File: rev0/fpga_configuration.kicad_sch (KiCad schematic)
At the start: 40 parts, among them IC1 ECP5-BGA256, J10 TC_SWD, J5 Conn_FPGA_JTAG_10, J6 Conn_ARM_JTAG_SWD_10, U6 ATSAMD11D14A-MUT, U7 W25Q32JVSS

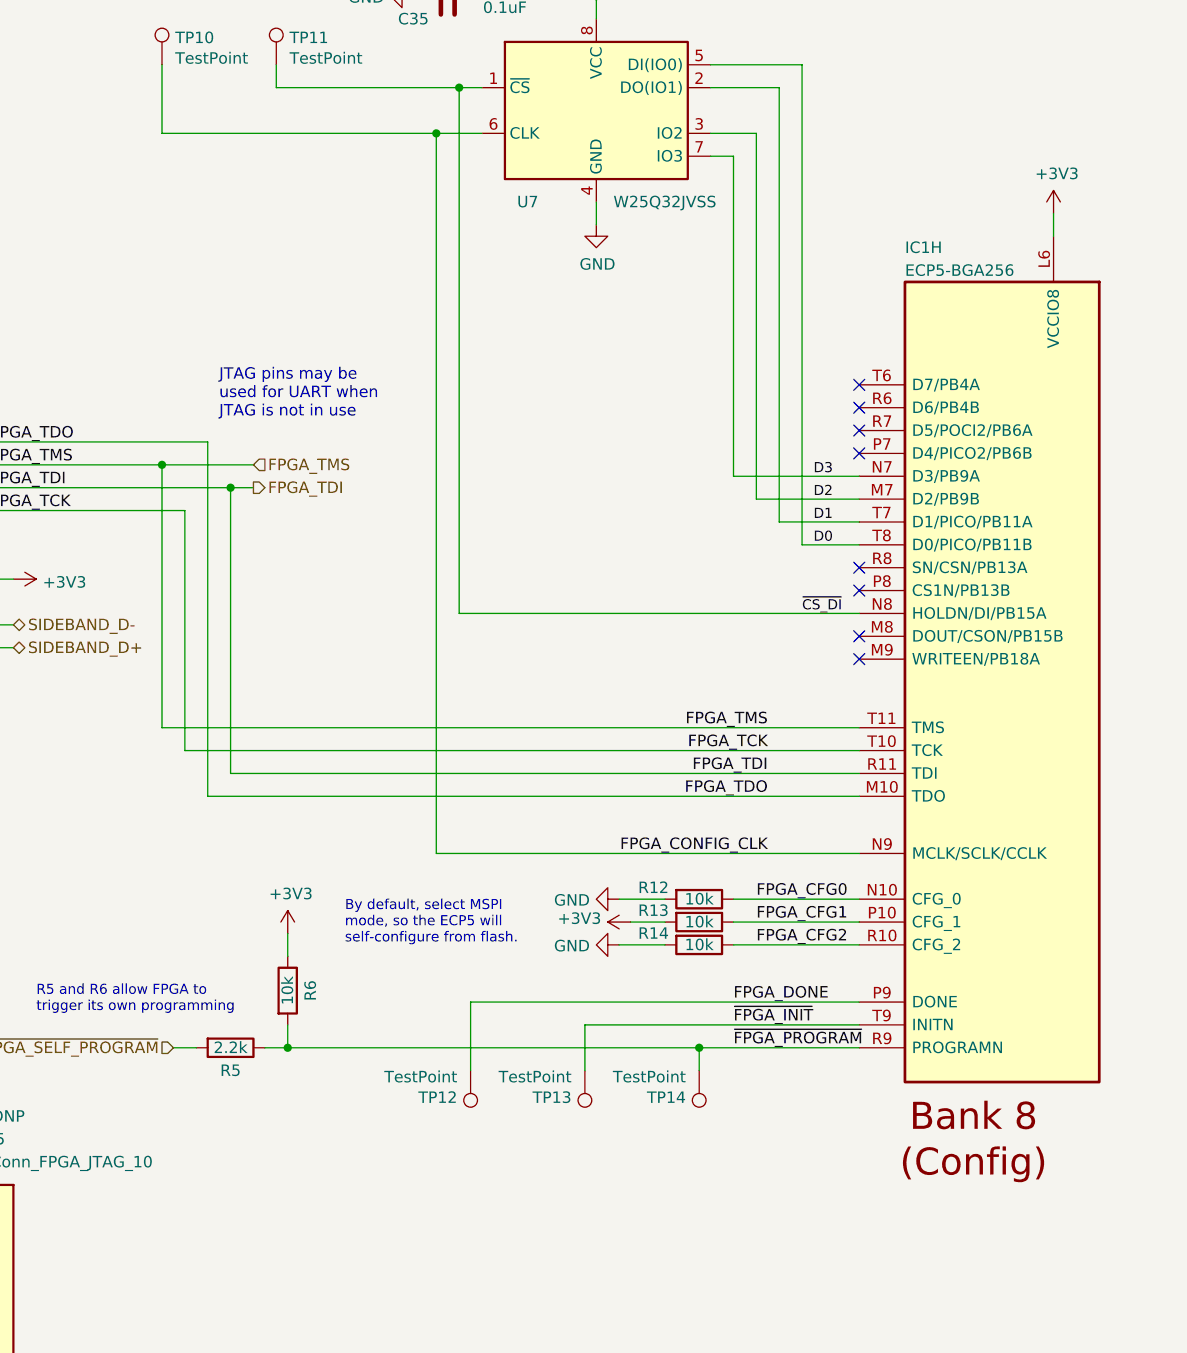
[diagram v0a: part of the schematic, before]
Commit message: hardware: add button BTN to FPGA
intended for SoC reset or alternative FPGA use
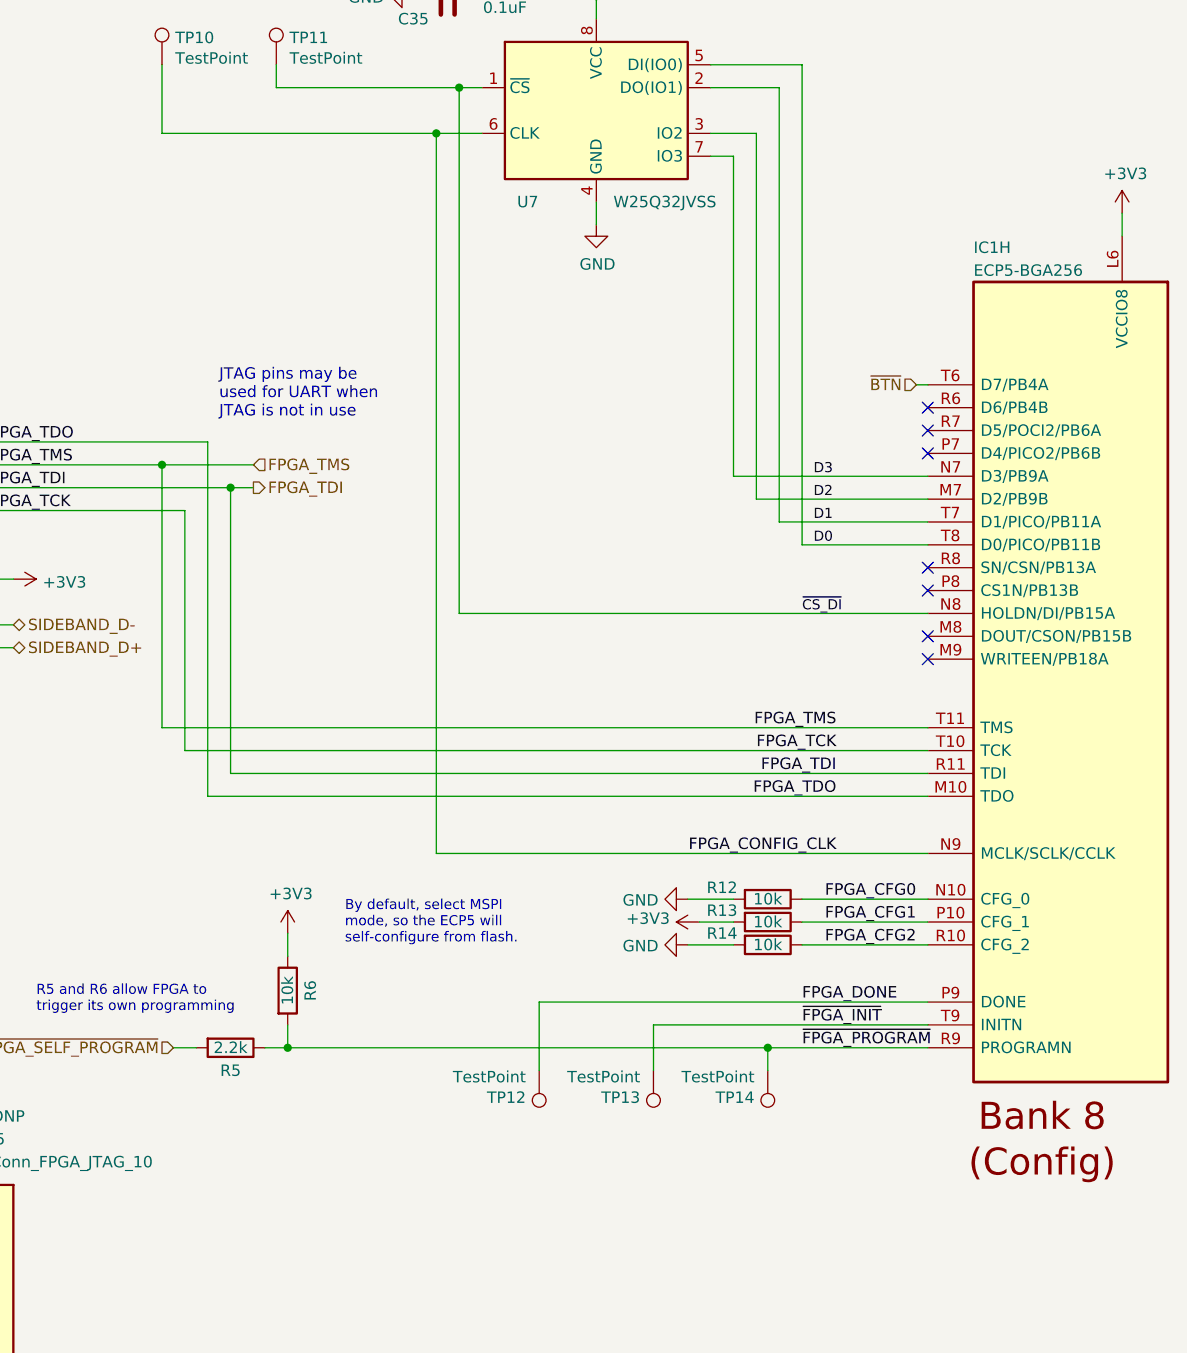
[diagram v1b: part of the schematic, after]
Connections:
- net ~{BTN}: now reaches IC1.T6 (D7/PB4A)
- no-connect marks 15 -> 14
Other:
- moved on the sheet: IC1H, R12, R13, R14, TP12, TP13, TP14

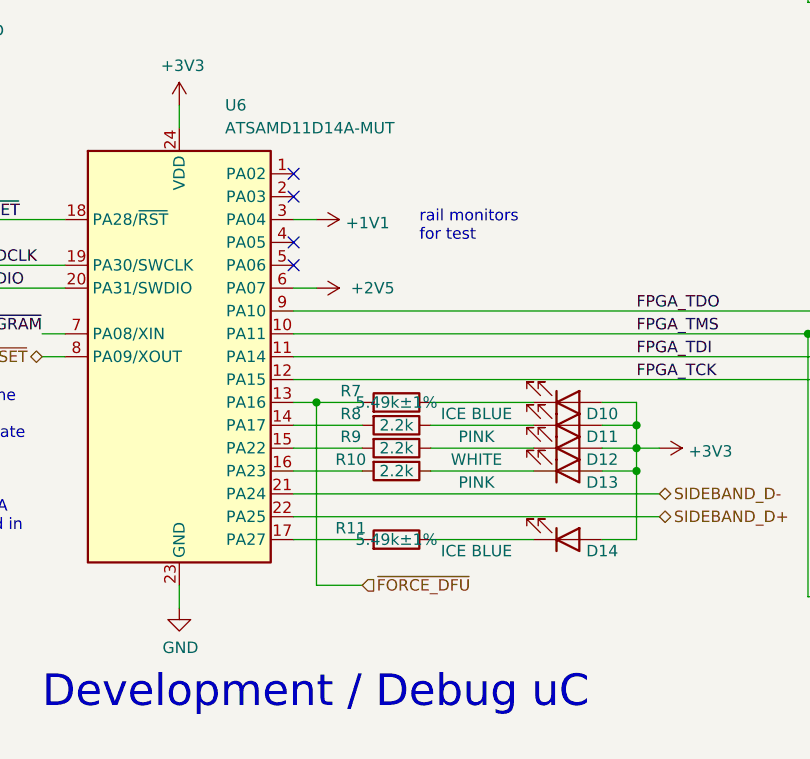
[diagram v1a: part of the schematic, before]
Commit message: hardware: move DFU button to its own pin
no longer shared with LED
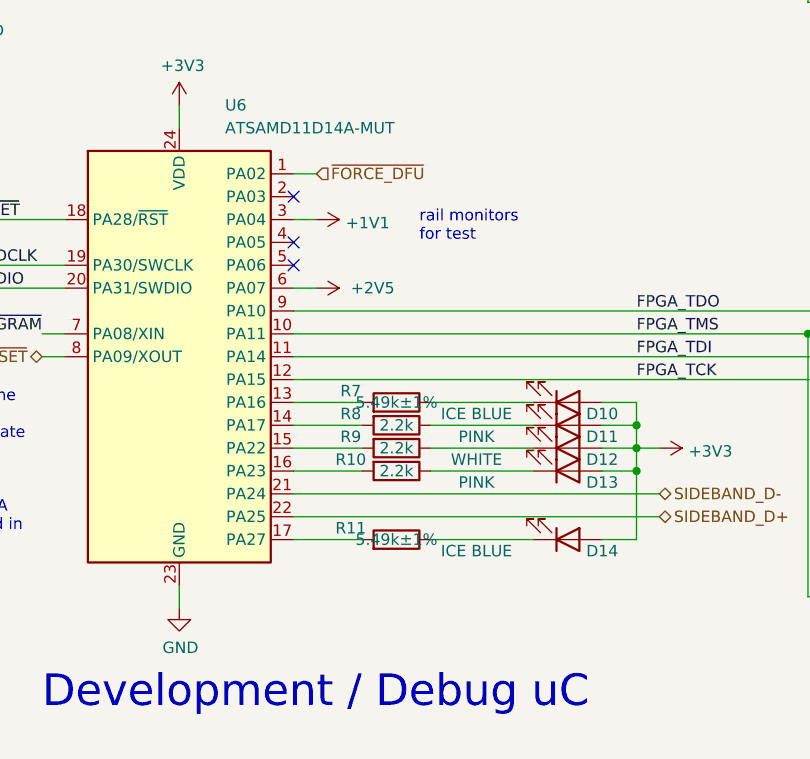
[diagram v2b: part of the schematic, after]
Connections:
- net ~{FORCE_DFU}: now also U6.1 (PA02); no longer R7.2, U6.13 (PA16)
- new net: R7.2, U6.13 (PA16)
- no-connect marks 14 -> 13
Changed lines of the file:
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@@
   (junction (at 62.23 27.94) (diameter 0) (color 0 0 0 0)
-  )
-  (junction (at 107.95 85.09) (diameter 0) (color 0 0 0 0)
   )
   (junction (at 170.18 80.01) (diameter 0) (color 0 0 0 0)
@@
   (no_connect (at 105.41 62.23))
   (no_connect (at 50.8 176.53))
-  (no_connect (at 105.41 59.69))
   (no_connect (at 123.19 162.56))
   (wire (pts (xy 247.65 142.24) (xy 229.87 142.24))
@@
     (stroke (width 0) (type default) (color 0 0 0 0))
   )
-  (wire (pts (xy 107.95 105.41) (xy 107.95 85.09))
-    (stroke (width 0) (type default) (color 0 0 0 0))
-  )
   (wire (pts (xy 170.18 80.01) (xy 172.72 80.01))
     (stroke (width 0) (type default) (color 0 0 0 0))
@@
     (stroke (width 0) (type default) (color 0 0 0 0))
   )
-  (wire (pts (xy 107.95 85.09) (xy 113.03 85.09))
+  (wire (pts (xy 105.41 85.09) (xy 113.03 85.09))
     (stroke (width 0) (type default) (color 0 0 0 0))
   )
@@
     (stroke (width 0) (type default) (color 0 0 0 0))
   )
-  (wire (pts (xy 105.41 85.09) (xy 107.95 85.09))
-    (stroke (width 0) (type default) (color 0 0 0 0))
-  )
   (wire (pts (xy 39.37 27.94) (xy 46.99 27.94))
     (stroke (width 0) (type default) (color 0 0 0 0))
   )
+  (wire (pts (xy 107.95 59.69) (xy 105.41 59.69))
+    (stroke (width 0) (type default) (color 0 0 0 0))
+  )
   (wire (pts (xy 162.56 33.02) (xy 162.56 40.64))
     (stroke (width 0) (type default) (color 0 0 0 0))
@@
   )
   (wire (pts (xy 45.72 64.77) (xy 63.5 64.77))
-    (stroke (width 0) (type default) (color 0 0 0 0))
-  )
-  (wire (pts (xy 107.95 105.41) (xy 113.03 105.41))
     (stroke (width 0) (type default) (color 0 0 0 0))
   )
@@
     (effects (font (size 1.27 1.27)) (justify left bottom))
   )
-  (hierarchical_label "~{FORCE_DFU}" (shape input) (at 113.03 105.41 0)
+  (hierarchical_label "~{FORCE_DFU}" (shape input) (at 107.95 59.69 0)
     (effects (font (size 1.27 1.27)) (justify left))
   )

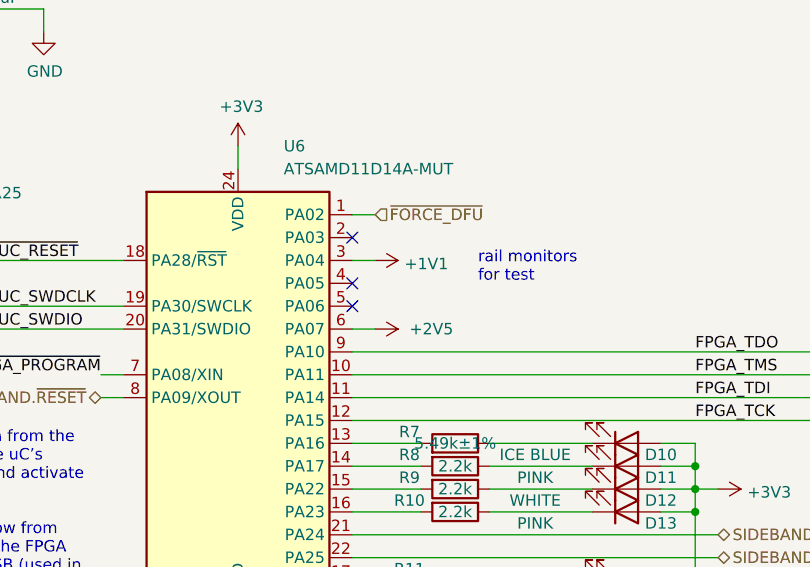
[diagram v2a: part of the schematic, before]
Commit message: hardware: move 2V5 measurement from PA07 to PA03
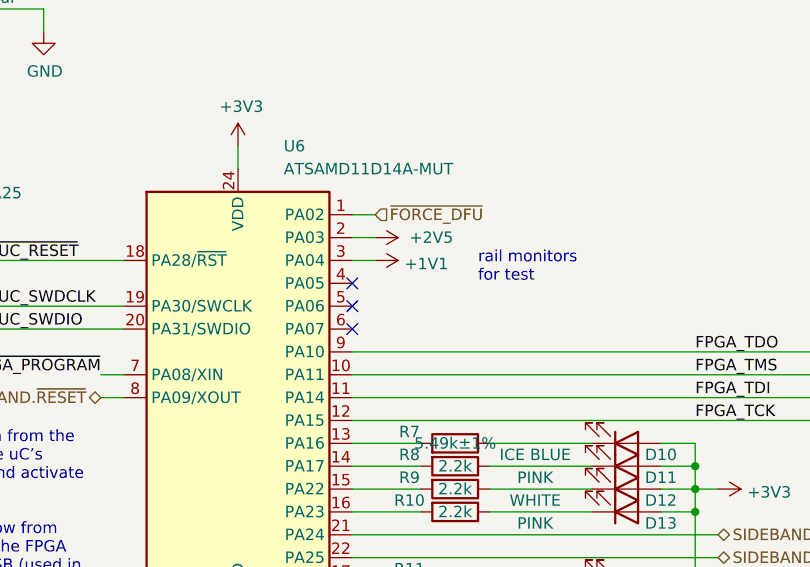
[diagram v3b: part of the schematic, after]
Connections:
- net +2V5: now also U6.2 (PA03); no longer U6.6 (PA07)
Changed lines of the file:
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@@
   (no_connect (at 247.65 73.66))
   (no_connect (at 50.8 173.99))
-  (no_connect (at 105.41 62.23))
+  (no_connect (at 105.41 72.39))
   (no_connect (at 50.8 176.53))
   (no_connect (at 123.19 162.56))
@@
     (stroke (width 0) (type default) (color 0 0 0 0))
   )
+  (wire (pts (xy 105.41 62.23) (xy 107.95 62.23))
+    (stroke (width 0) (type default) (color 0 0 0 0))
+  )
   (wire (pts (xy 45.72 135.89) (xy 45.72 163.83))
     (stroke (width 0) (type default) (color 0 0 0 0))
@@
   )
   (wire (pts (xy 63.5 153.67) (xy 63.5 156.21))
-    (stroke (width 0) (type default) (color 0 0 0 0))
-  )
-  (wire (pts (xy 105.41 72.39) (xy 107.95 72.39))
     (stroke (width 0) (type default) (color 0 0 0 0))
   )
@@
     (pin "1")
   )
-  (symbol (lib_id "power:+2V5") (at 107.95 72.39 270) (unit 1)
-    (in_bom yes) (on_board yes)
-    (property "Reference" "#PWR046" (id 0) (at 104.14 72.39 0)
-      (effects (font (size 1.27 1.27)) hide)
-    )
-    (property "Value" "+2V5" (id 1) (at 111.76 72.39 90)
+  (symbol (lib_id "power:+2V5") (at 107.95 62.23 270) (unit 1)
+    (in_bom yes) (on_board yes)
+    (property "Reference" "#PWR046" (id 0) (at 104.14 62.23 0)
+      (effects (font (size 1.27 1.27)) hide)
+    )
+    (property "Value" "+2V5" (id 1) (at 111.76 62.23 90)
       (effects (font (size 1.27 1.27)) (justify left))
     )
-    (property "Footprint" "" (id 2) (at 107.95 72.39 0)
-      (effects (font (size 1.27 1.27)) hide)
-    )
-    (property "Datasheet" "" (id 3) (at 107.95 72.39 0)
-      (effects (font (size 1.27 1.27)) hide)
-    )
+    (property "Footprint" "" (id 2) (at 107.95 62.23 0)
+      (effects (font (size 1.27 1.27)) hide)
+    )
+    (property "Datasheet" "" (id 3) (at 107.95 62.23 0)
+      (effects (font (size 1.27 1.27)) hide)
+    )
